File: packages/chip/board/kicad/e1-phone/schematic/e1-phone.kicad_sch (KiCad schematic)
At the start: 0 parts

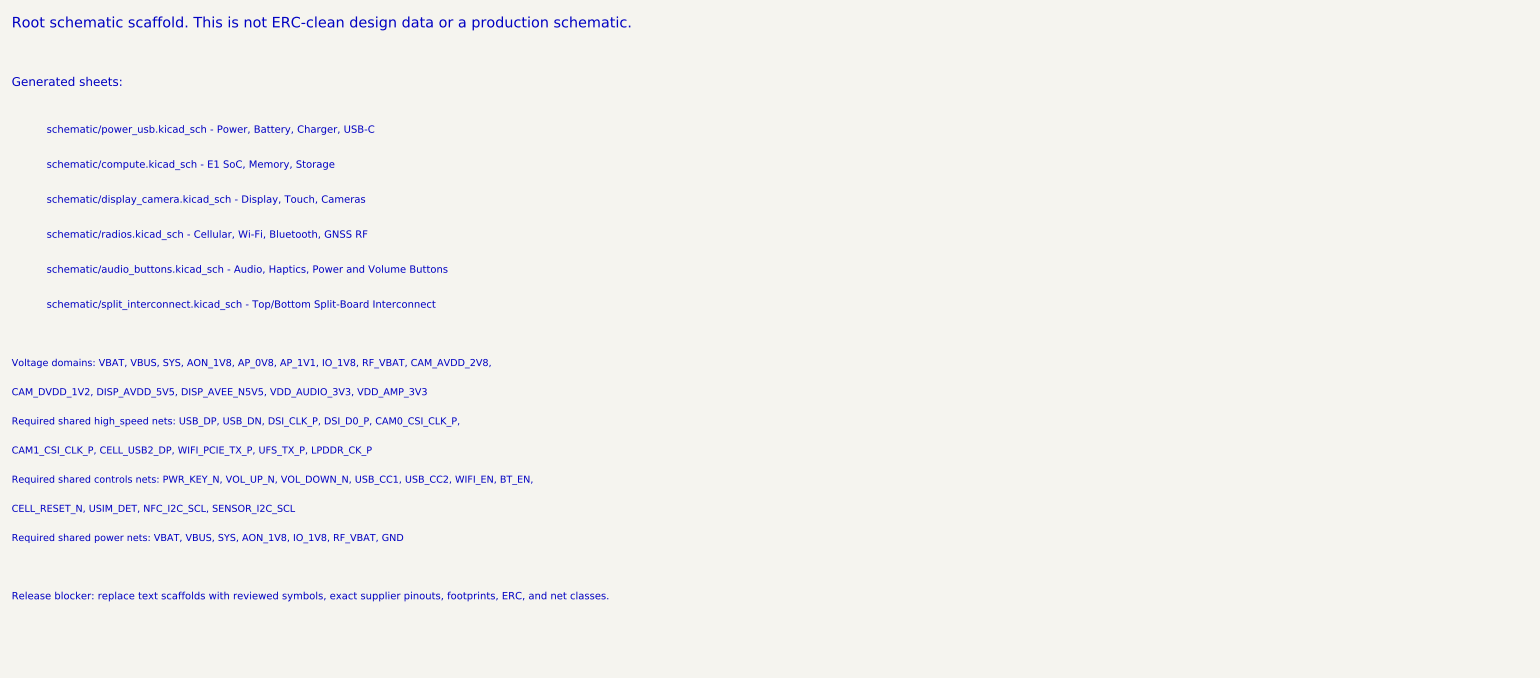
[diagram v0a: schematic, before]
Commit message: chip(e1-phone): re-render exploded animation with corrected framing + lighting + EGL chunking
Visual self-review of the previous render exposed three defects that this commit closes:

- Camera was at radius 220 mm with 35deg yfov; phone is ~155 mm tall with parts that fly ~150 mm outward at peak explode, so the camera was effectively inside the explosion bubble. Bumped radius to 500 mm and narrowed yfov to 28deg; tilt to 15deg.
- Lights were camera-anchored, so the back of the orange shell went muddy during the 360deg orbit. Switched to world-anchored 3-point lighting.
- pyrender EGL leaked GPU memory and consistently died around frame ~150. Recreating OffscreenRenderer every 30 frames keeps the full 360-frame render stable.

Re-render output (all confirmed by reading 4 keyframes):
- e1-phone-exploded.mp4: 1920x1080, 30 fps, 12 s, h264/yuv420p, 897 KB
- e1-phone-exploded.glb: 98 nodes, 97 meshes, 3 clips (explode/reassemble/turntable), 183 KB
- e1-phone-exploded-frames/: 360 sequential frames + 24 keyframes at 0.5 s

Also restores the chip e1-phone artifacts (mechanical, board, supplier-pinouts, generator scripts) that an out-of-band git reset to origin/develop wiped between my previous commits ae3f83e9e7 / bd0a350198 and the current HEAD.

Co-Authored-By: Claude Opus 4.7 (1M context) <noreply@anthropic.com>
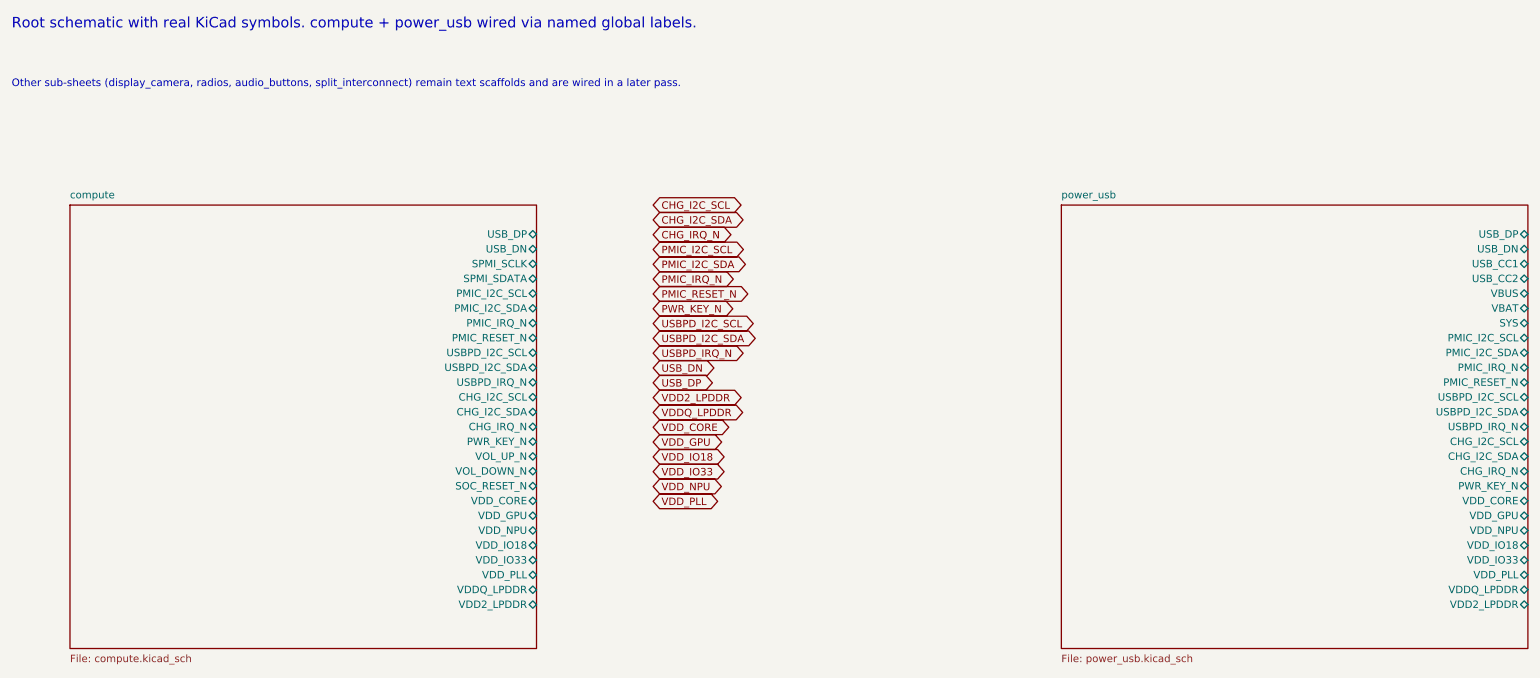
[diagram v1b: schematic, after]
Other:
- added sheet compute (compute.kicad_sch)
- added sheet power_usb (power_usb.kicad_sch)
- note added: "Other sub-sheets (display_camera, radios, audio_buttons, split_interconnect) remain text scaffolds and are wired in a later pass."
- note added: "Root schematic with real KiCad symbols. compute + power_usb wired via named global labels."
- note removed: "CAM1_CSI_CLK_P, CELL_USB2_DP, WIFI_PCIE_TX_P, UFS_TX_P, LPDDR_CK_P"
- note removed: "CAM_DVDD_1V2, DISP_AVDD_5V5, DISP_AVEE_N5V5, VDD_AUDIO_3V3, VDD_AMP_3V3"
- note removed: "CELL_RESET_N, USIM_DET, NFC_I2C_SCL, SENSOR_I2C_SCL"
- note removed: "Generated sheets:"
- note removed: "Release blocker: replace text scaffolds with reviewed symbols, exact supplier pinouts, footprints, ERC, and net classes."
- note removed: "Required shared controls nets: PWR_KEY_N, VOL_UP_N, VOL_DOWN_N, USB_CC1, USB_CC2, WIFI_EN, BT_EN,"
- note removed: "Required shared high_speed nets: USB_DP, USB_DN, DSI_CLK_P, DSI_D0_P, CAM0_CSI_CLK_P,"
- note removed: "Required shared power nets: VBAT, VBUS, SYS, AON_1V8, IO_1V8, RF_VBAT, GND"
- note removed: "Root schematic scaffold. This is not ERC-clean design data or a production schematic."
- note removed: "Voltage domains: VBAT, VBUS, SYS, AON_1V8, AP_0V8, AP_1V1, IO_1V8, RF_VBAT, CAM_AVDD_2V8,"
- note removed: "schematic/audio_buttons.kicad_sch - Audio, Haptics, Power and Volume Buttons"
- note removed: "schematic/compute.kicad_sch - E1 SoC, Memory, Storage"
- note removed: "schematic/display_camera.kicad_sch - Display, Touch, Cameras"
- note removed: "schematic/power_usb.kicad_sch - Power, Battery, Charger, USB-C"
- note removed: "schematic/radios.kicad_sch - Cellular, Wi-Fi, Bluetooth, GNSS RF"
- note removed: "schematic/split_interconnect.kicad_sch - Top/Bottom Split-Board Interconnect"
- title: E1 Phone Mainboard - schematic scaffold -> E1 Phone Mainboard - root schematic
